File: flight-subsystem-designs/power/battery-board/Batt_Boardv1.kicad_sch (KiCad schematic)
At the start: 42 parts, among them J1 Conn_02x26_Odd_Even, J2 Conn_02x26_Odd_Even, Q1 IRF7458, Q2 IRF7458, U1 R5460N210AD1, U2 BQ29200DRBR, U3 TLA2024IRUGR, U4 LM35-LP, U5 LM35-LP, U6 LM35-LP, U7 LM35-LP

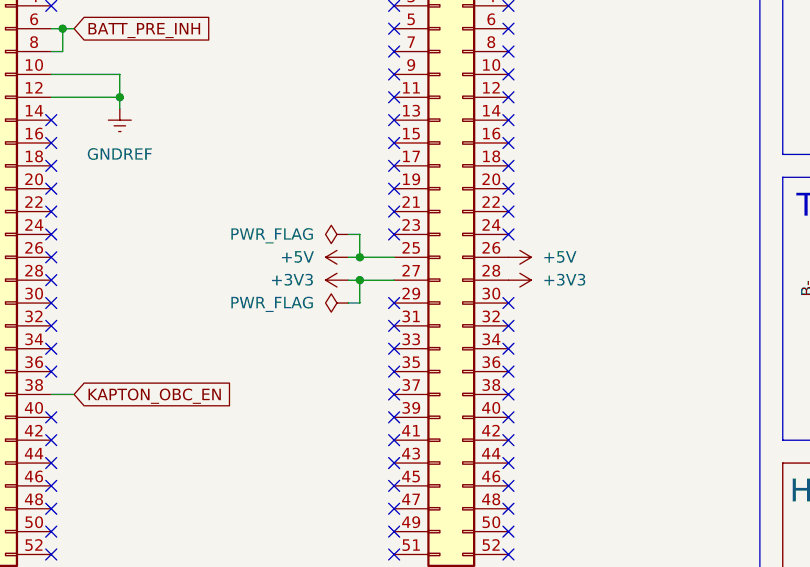
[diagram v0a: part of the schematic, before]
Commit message: clear up drcs; make pour clearance larger; optimize a bit
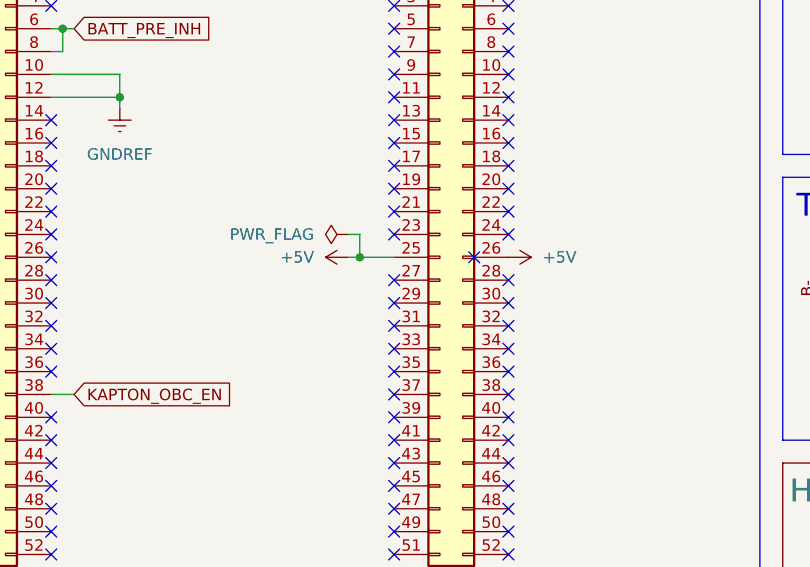
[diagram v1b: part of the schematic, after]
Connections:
- net +3V3: no longer names the net of J2.27 (Pin_27)
- net +3V3: no longer J2.28 (Pin_28)
- no-connect marks 92 -> 95
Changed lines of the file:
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@@
 	)
 	(junction
-		(at 85.09 63.5)
-		(diameter 0)
-		(color 0 0 0 0)
-	)
-	(junction
 		(at 88.9 116.84)
 		(diameter 0)
@@
 	)
 	(no_connect
+		(at 101.6 63.5)
+	)
+	(no_connect
 		(at 50.8 30.48)
 	)
@@
 	)
 	(no_connect
+		(at 88.9 63.5)
+	)
+	(no_connect
 		(at 88.9 81.28)
 	)
 	(no_connect
+		(at 97.79 60.96)
+	)
+	(no_connect
 		(at 50.8 83.82)
 	)
@@
 	(wire
 		(pts
-			(xy 83.82 63.5) (xy 85.09 63.5)
-		)
-		(stroke
-			(width 0)
-			(type default)
-		)
-	)
-	(wire
-		(pts
 			(xy 36.83 121.92) (xy 58.42 121.92)
 		)
@@
 	(wire
 		(pts
-			(xy 85.09 66.04) (xy 85.09 63.5)
-		)
-		(stroke
-			(width 0)
-			(type default)
-		)
-	)
-	(wire
-		(pts
 			(xy 113.03 127) (xy 113.03 124.46)
 		)
@@
 	(wire
 		(pts
-			(xy 83.82 66.04) (xy 85.09 66.04)
-		)
-		(stroke
-			(width 0)
-			(type default)
-		)
-	)
-	(wire
-		(pts
 			(xy 209.55 86.36) (xy 209.55 102.87)
 		)
@@
 	(wire
 		(pts
-			(xy 85.09 63.5) (xy 88.9 63.5)
-		)
-		(stroke
-			(width 0)
-			(type default)
-		)
-	)
-	(wire
-		(pts
 			(xy 241.3 140.97) (xy 274.32 140.97)
 		)
@@
 	)
 	(symbol
-		(lib_id "power:+3V3")
-		(at 83.82 63.5 90)
-		(unit 1)
-		(exclude_from_sim no)
-		(in_bom yes)
-		(on_board yes)
-		(dnp no)
-		(fields_autoplaced yes)
-		(property "Reference" "#PWR05"
-			(at 87.63 63.5 0)
-			(effects
-				(font
-					(size 1.27 1.27)
-				)
-				(hide yes)
-			)
-		)
-		(property "Value" "+3V3"
-			(at 80.01 63.4999 90)
-			(effects
-				(font
-					(size 1.27 1.27)
-				)
-				(justify left)
-			)
-		)
-		(property "Footprint" ""
-			(at 83.82 63.5 0)
-			(effects
-				(font
-					(size 1.27 1.27)
-				)
-				(hide yes)
-			)
-		)
-		(property "Datasheet" ""
-			(at 83.82 63.5 0)
-			(effects
-				(font
-					(size 1.27 1.27)
-				)
-				(hide yes)
-			)
-		)
-		(property "Description" "Power symbol creates a global label with name \"+3V3\""
-			(at 83.82 63.5 0)
-			(effects
-				(font
-					(size 1.27 1.27)
-				)
-				(hide yes)
-			)
-		)
-		(pin "1"
-		)
-		(instances
-			(project ""
-				(path "/a5e22de5-0e9e-4e3b-9cf5-d999de47cef4"
-					(reference "#PWR05")
-					(unit 1)
-				)
-			)
-		)
-	)
-	(symbol
 		(lib_id "254TR-18650:254TR-18650")
 		(at 201.93 25.4 180)
@@
 	)
 	(symbol
-		(lib_id "power:+3V3")
-		(at 101.6 63.5 270)
-		(unit 1)
-		(exclude_from_sim no)
-		(in_bom yes)
-		(on_board yes)
-		(dnp no)
-		(fields_autoplaced yes)
-		(property "Reference" "#PWR07"
-			(at 97.79 63.5 0)
-			(effects
-				(font
-					(size 1.27 1.27)
-				)
-				(hide yes)
-			)
-		)
-		(property "Value" "+3V3"
-			(at 105.41 63.4999 90)
-			(effects
-				(font
-					(size 1.27 1.27)
-				)
-				(justify left)
-			)
-		)
-		(property "Footprint" ""
-			(at 101.6 63.5 0)
-			(effects
-				(font
-					(size 1.27 1.27)
-				)
-				(hide yes)
-			)
-		)
-		(property "Datasheet" ""
-			(at 101.6 63.5 0)
-			(effects
-				(font
-					(size 1.27 1.27)
-				)
-				(hide yes)
-			)
-		)
-		(property "Description" "Power symbol creates a global label with name \"+3V3\""
-			(at 101.6 63.5 0)
-			(effects
-				(font
-					(size 1.27 1.27)
-				)
-				(hide yes)
-			)
-		)
-		(pin "1"
-		)
-		(instances
-			(project ""
-				(path "/a5e22de5-0e9e-4e3b-9cf5-d999de47cef4"
-					(reference "#PWR07")
-					(unit 1)
-				)
-			)
-		)
-	)
-	(symbol
 		(lib_id "power:GNDREF")
 		(at 162.56 139.7 0)
@@
 					(unit 1)
 				)
-			)
-		)
-	)
-	(symbol
-		(lib_id "power:PWR_FLAG")
-		(at 83.82 66.04 90)
-		(unit 1)
-		(exclude_from_sim no)
-		(in_bom yes)
-		(on_board yes)
-		(dnp no)
-		(fields_autoplaced yes)
-		(property "Reference" "#FLG03"
-			(at 81.915 66.04 0)
-			(effects
-				(font
-					(size 1.27 1.27)
-				)
-				(hide yes)
-			)
-		)
-		(property "Value" "PWR_FLAG"
-			(at 80.01 66.0399 90)
-			(effects
-				(font
-					(size 1.27 1.27)
-				)
-				(justify left)
-			)
-		)
-		(property "Footprint" ""
-			(at 83.82 66.04 0)
-			(effects
-				(font
-					(size 1.27 1.27)
-				)
-				(hide yes)
-			)
-		)
-		(property "Datasheet" "~"
-			(at 83.82 66.04 0)
-			(effects
-				(font
-					(size 1.27 1.27)
-				)
-				(hide yes)
-			)
-		)
-		(property "Description" "Special symbol for telling ERC where power comes from"
-			(at 83.82 66.04 0)
-			(effects
-				(font
-					(size 1.27 1.27)
-				)
-				(hide yes)
-			)
-		)
-		(pin "1"
-		)
-		(instances
-			(project ""
-				(path "/a5e22de5-0e9e-4e3b-9cf5-d999de47cef4"
-					(reference "#FLG03")
-					(unit 1)
-				)

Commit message: reroute
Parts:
- added TP5: TestPoint, TestPoint:TestPoint_Loop_D1.80mm_Drill1.0mm_Beaded, symbol Connector:TestPoint
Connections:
- net KAPTON_SEL: now also J1.36 (Pin_36); no longer J2.1 (Pin_1)
- new net +5VA: TP5.1
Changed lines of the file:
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@@
 	)
 	(no_connect
-		(at 50.8 73.66)
-	)
-	(no_connect
 		(at 101.6 76.2)
 	)
@@
 	)
 	(no_connect
+		(at 88.9 30.48)
+	)
+	(no_connect
 		(at 101.6 53.34)
 	)
@@
 	(wire
 		(pts
-			(xy 86.36 30.48) (xy 88.9 30.48)
+			(xy 50.8 73.66) (xy 53.34 73.66)
 		)
 		(stroke
@@
 	(global_label "KAPTON_SEL"
 		(shape input)
-		(at 86.36 30.48 180)
+		(at 53.34 73.66 0)
 		(fields_autoplaced yes)
 		(effects
@@
 				(size 1.27 1.27)
 			)
-			(justify right)
+			(justify left)
 		)
 		(property "Intersheetrefs" "${INTERSHEET_REFS}"
-			(at 71.7634 30.48 0)
+			(at 67.9366 73.66 0)
 			(effects
 				(font
 					(size 1.27 1.27)
 				)
-				(justify right)
+				(justify left)
 				(hide yes)
 			)
@@
 	)
 	(symbol
+		(lib_id "power:+5VA")
+		(at 135.89 74.93 0)
+		(unit 1)
+		(exclude_from_sim no)
+		(in_bom yes)
+		(on_board yes)
+		(dnp no)
+		(property "Reference" "#PWR05"
+			(at 135.89 78.74 0)
+			(effects
+				(font
+					(size 1.27 1.27)
+				)
+				(hide yes)
+			)
+		)
+		(property "Value" "+5VA"
+			(at 135.382 71.374 0)
+			(effects
+				(font
+					(size 1.27 1.27)
+				)
+			)
+		)
+		(property "Footprint" ""
+			(at 135.89 74.93 0)
+			(effects
+				(font
+					(size 1.27 1.27)
+				)
+				(hide yes)
+			)
+		)
+		(property "Datasheet" ""
+			(at 135.89 74.93 0)
+			(effects
+				(font
+					(size 1.27 1.27)
+				)
+				(hide yes)
+			)
+		)
+		(property "Description" "Power symbol creates a global label with name \"+5VA\""
+			(at 135.89 74.93 0)
+			(effects
+				(font
+					(size 1.27 1.27)
+				)
+				(hide yes)
+			)
+		)
+		(pin "1"
+		)
+		(instances
+			(project ""
+				(path "/a5e22de5-0e9e-4e3b-9cf5-d999de47cef4"
+					(reference "#PWR05")
+					(unit 1)
+				)
+			)
+		)
+	)
+	(symbol
 		(lib_id "power:GNDREF")
 		(at 179.07 134.62 0)
@@
 					(unit 1)
 				)
+			)
+		)
+	)
+	(symbol
+		(lib_id "Connector:TestPoint")
+		(at 135.89 74.93 180)
+		(unit 1)
+		(exclude_from_sim no)
+		(in_bom yes)
+		(on_board yes)
+		(dnp no)
+		(property "Reference" "TP5"
+			(at 140.716 78.232 0)
+			(effects
+				(font
+					(size 1.27 1.27)
+				)
+				(justify left)
+			)
+		)
+		(property "Value" "TestPoint"
+			(at 134.4168 75.6158 0)
+			(effects
+				(font
+					(size 1.27 1.27)
+				)
+				(justify left)
+				(hide yes)
+			)
+		)
+		(property "Footprint" "TestPoint:TestPoint_Loop_D1.80mm_Drill1.0mm_Beaded"
+			(at 130.81 74.93 0)
+			(effects
+				(font
+					(size 1.27 1.27)
+				)
+				(hide yes)
+			)
+		)
+		(property "Datasheet" "~"
+			(at 130.81 74.93 0)
+			(effects
+				(font
+					(size 1.27 1.27)
+				)
+				(hide yes)
+			)
+		)
+		(property "Description" ""
+			(at 135.89 74.93 0)
+			(effects
+				(font
+					(size 1.27 1.27)
+				)
+				(hide yes)
+			)
+		)
+		(pin "1"
+		)
+		(instances
+			(project "Batt_Boardv1"
+				(path "/a5e22de5-0e9e-4e3b-9cf5-d999de47cef4"
+					(reference "TP5")
+					(unit 1)
+				)
